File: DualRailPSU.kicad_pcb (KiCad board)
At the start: 2 copper layers, 76.2 x 96.5 mm, 24 parts, among them J1 Screw_Terminal_01x02, J2 1-726386-2, J3 Screw_Terminal_01x03

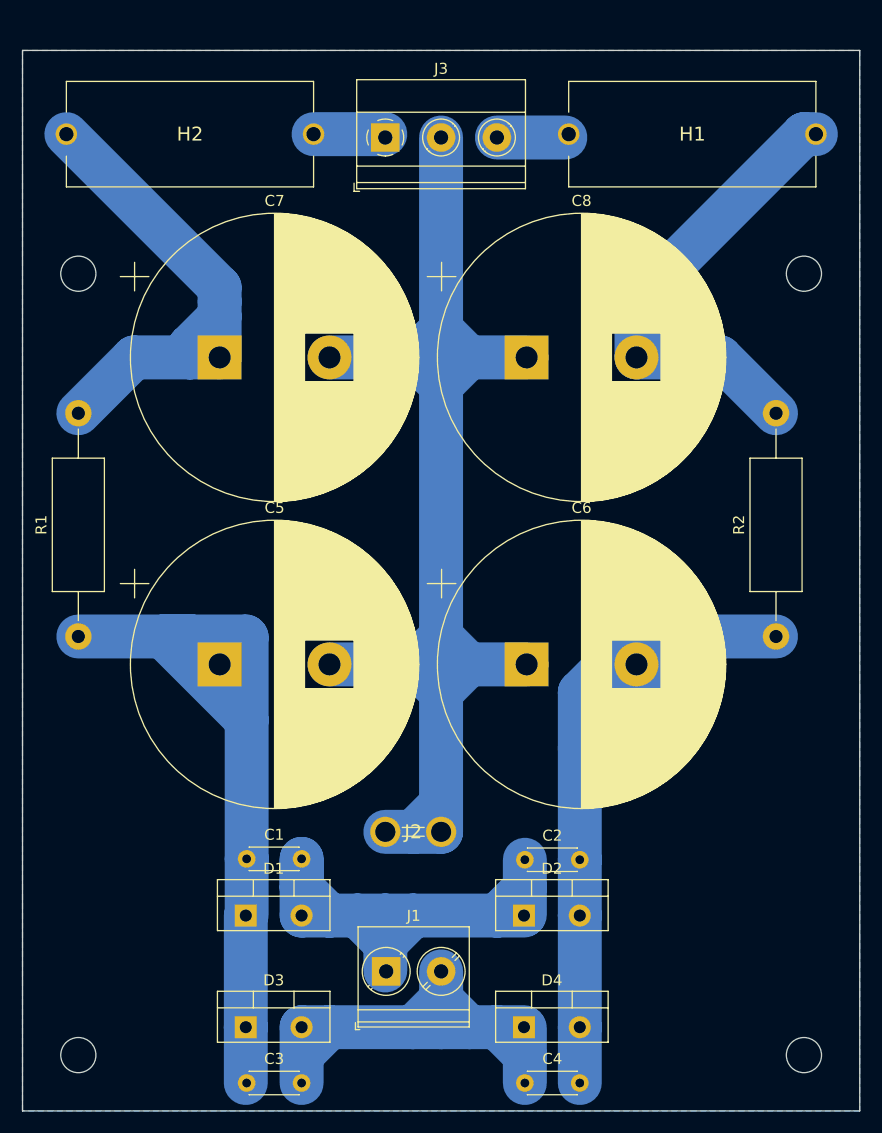
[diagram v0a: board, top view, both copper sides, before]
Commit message: Fixed output terminal block orientation, and moved text and logo to silscreen front layer
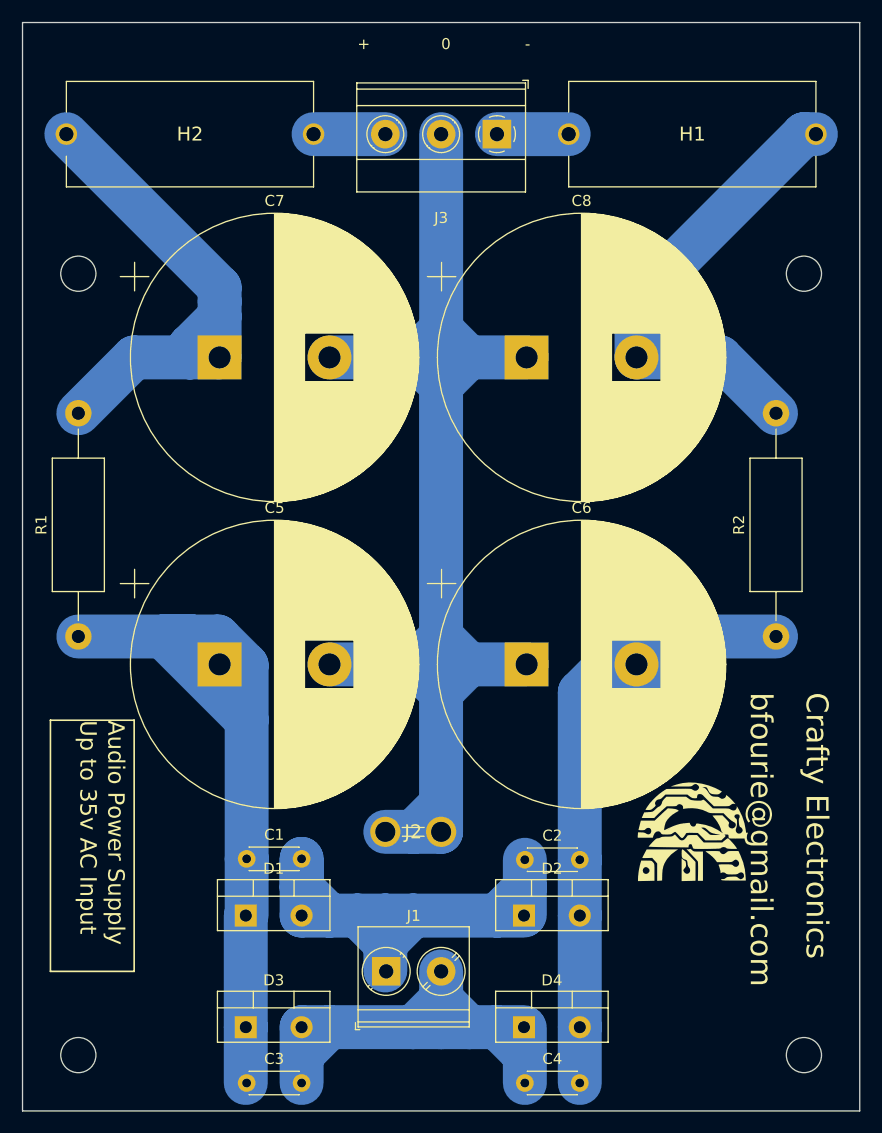
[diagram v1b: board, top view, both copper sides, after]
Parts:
- removed ?: LOGO, LOGO
- added G***: LOGO, LOGO, F.Cu at (106.7, 116.8)
- H1, H2: value 65600001009 -> Fuse Holder
- moved J3 10.2 mm to (88.9, 53.3), turned to 180 degrees
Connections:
- net /GND renamed 0
- J3 pad 1: /POS_Out -> /NEG_Out
- J3 pad 3: /NEG_Out -> /POS_Out
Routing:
- net 0: track 136.5 -> 139.3 mm
- net /POS_Rail: track 73.0 -> 71.5 mm
- removed copper zone on B.Cu, net 0
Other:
- board size 76.2 x 96.5 mm -> 76.2 x 99.1 mm
- board text added: "+"
- board text added: "-"
- board text added: "0"
- board text added: "Audio Power Supply"
- board text added: "Crafty Electronics"
- board text added: "Up to 35v AC Input"
- board text added: "bfourie@gmail.com"
